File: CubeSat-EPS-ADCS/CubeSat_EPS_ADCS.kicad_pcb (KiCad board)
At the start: 2 copper layers, 92 x 92 mm, 14 parts, among them J1 Conn_01x02_Pin, J2 Conn_01x03_Pin, J3 Conn_01x08_Pin, J4 Conn_01x02_Pin, J5 Screw_Terminal_01x02, J6 Screw_Terminal_01x02, J7 Screw_Terminal_01x02, U1 DRV8833 Module, U2 DRV8833 Module, U4 Buck_LM2596

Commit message: Mostly fine tuning the boards, also added capacitor for battery ADC
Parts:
- added G***: LOGO, Logos:HighVoltage, F.Cu at (142.6, 80.5)
- moved G*** 0.73 mm to (133.0, 138.7)
- moved U4 0.11 mm to (135.1, 61.9)
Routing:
- net GND: track 110.6 -> 131.1 mm
- net VCC_5V: track 14.9 -> 16.2 mm
- net VCC_8.4V_ADCS: track 30.9 -> 31.4 mm
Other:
- board text added: "-Buck LM2596"
- board text added: "-DRV8833"
- board text added: "-Motor 1"
- board text added: "-Motor 2"
- board text added: "-Motor 3"
- board text added: "5V | 1A"
- board text added: "G"
- board text added: "Overvoltage Protection"
- board text added: "S1"
- board text added: "S2"
- board text added: "S3"
- board text added: "S4"
- board text added: "S5"
- board text added: "S6"
- board text added: "VCC"
- board text removed: "M1 M2 M3"
- board text removed: "PWM1"
- board text removed: "PWM2"
- board text removed: "Vm1"
- board text removed: "Vm2"
- board text removed: "Vm3"

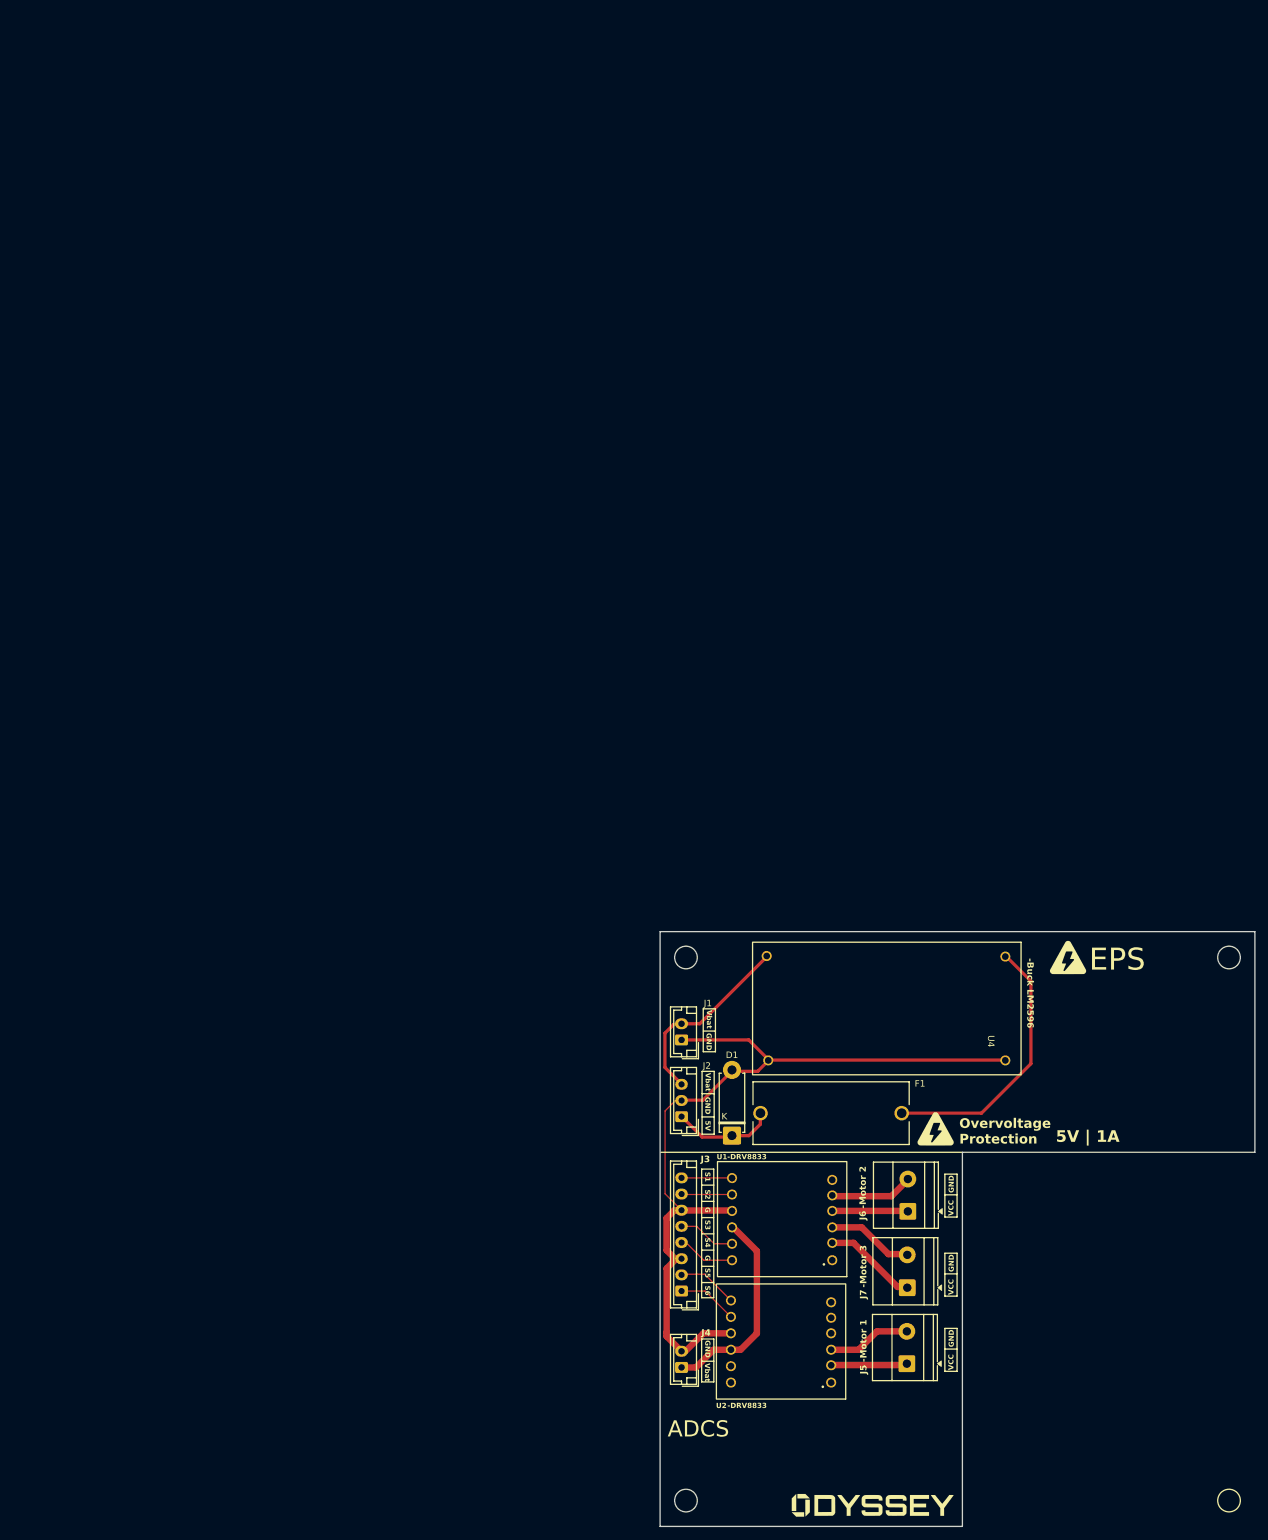
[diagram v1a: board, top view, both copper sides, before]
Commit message: Changing the size of all traces to fit the 1 mm requirement of the draft PCB
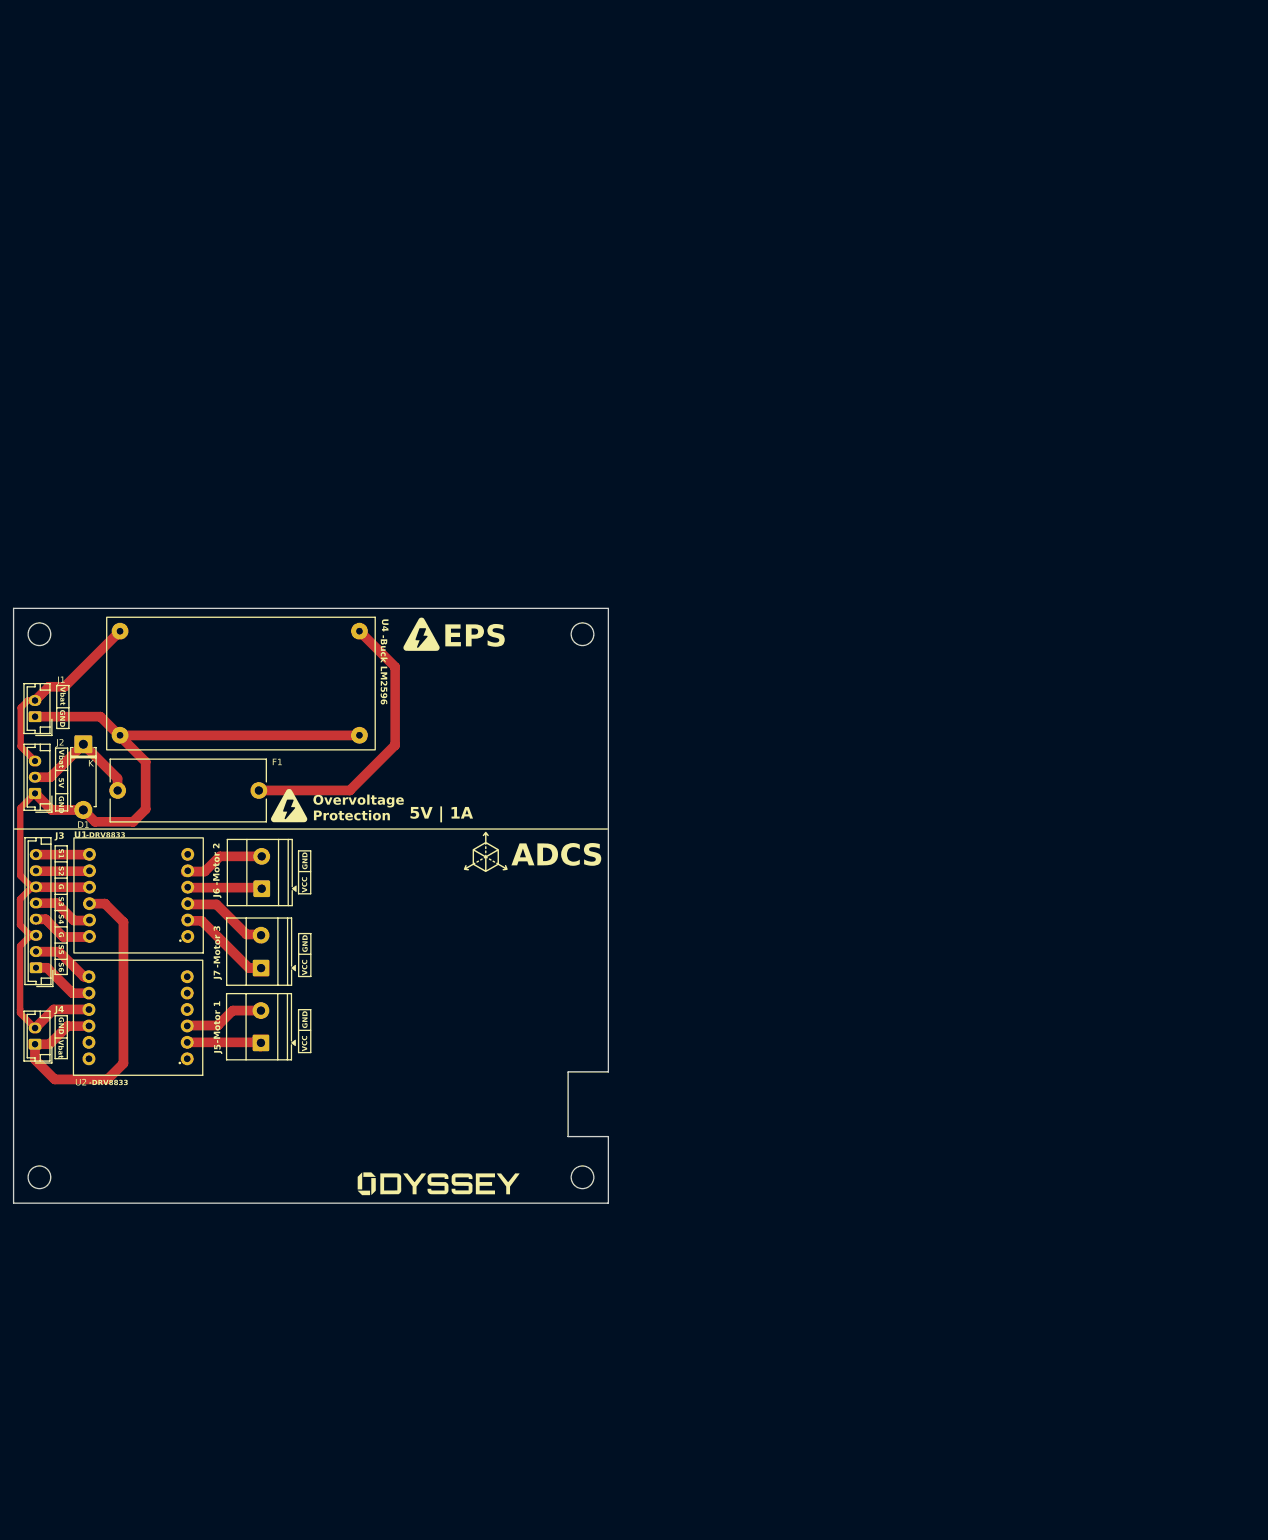
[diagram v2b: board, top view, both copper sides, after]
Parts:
- added G***: LOGO, Logos:Axys, F.Cu at (73.0, 37.7)
- moved D1 117.2 mm to (10.8, 21.0), turned to -90 degrees
- moved U4 111.8 mm to (35.2, 11.6)
- moved G*** 111.8 mm to (42.6, 30.5)
- moved G*** 111.8 mm to (63.1, 4.00)
- moved J1 111.8 mm to (3.32, 16.8)
- moved J2 111.8 mm to (3.32, 28.6)
- moved J4 111.8 mm to (3.32, 67.4)
- moved J6 111.7 mm to (38.4, 43.4)
- moved J3 111.7 mm to (3.47, 55.6)
- moved J5 111.6 mm to (38.3, 67.2)
- moved J7 111.5 mm to (38.3, 55.6)
- moved U1 111.4 mm to (19.3, 44.4)
- moved U2 111.3 mm to (19.3, 63.3)
- moved F1 111.3 mm to (27.0, 28.2)
- moved G*** 83.6 mm to (65.8, 89.0)
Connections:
- J2 pad 1: VCC_5V -> GND
- J2 pad 2: GND -> VCC_5V
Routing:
- net VCC_8.4V_ADCS: track 31.4 -> 56.2 mm
- net GND: track 131.1 -> 147.3 mm
- net VCC_5V: track 16.2 -> 19.0 mm
- net Net-(U4-Vout): track 41.4 -> 44.0 mm
- net VCC_M2: track 12.5 -> 11.3 mm
- net M1_PWM2: track 9.30 -> 9.97 mm
- net M2_PWM2: track 8.94 -> 9.60 mm
- net M2_PWM1: track 8.92 -> 9.58 mm
- net M1_PWM1: track 9.37 -> 9.95 mm
- net VCC_8.4V_EPS: track 29.9 -> 29.4 mm
- net GND_M1: track 12.9 -> 12.4 mm
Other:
- outline, holes or cut-outs redrawn

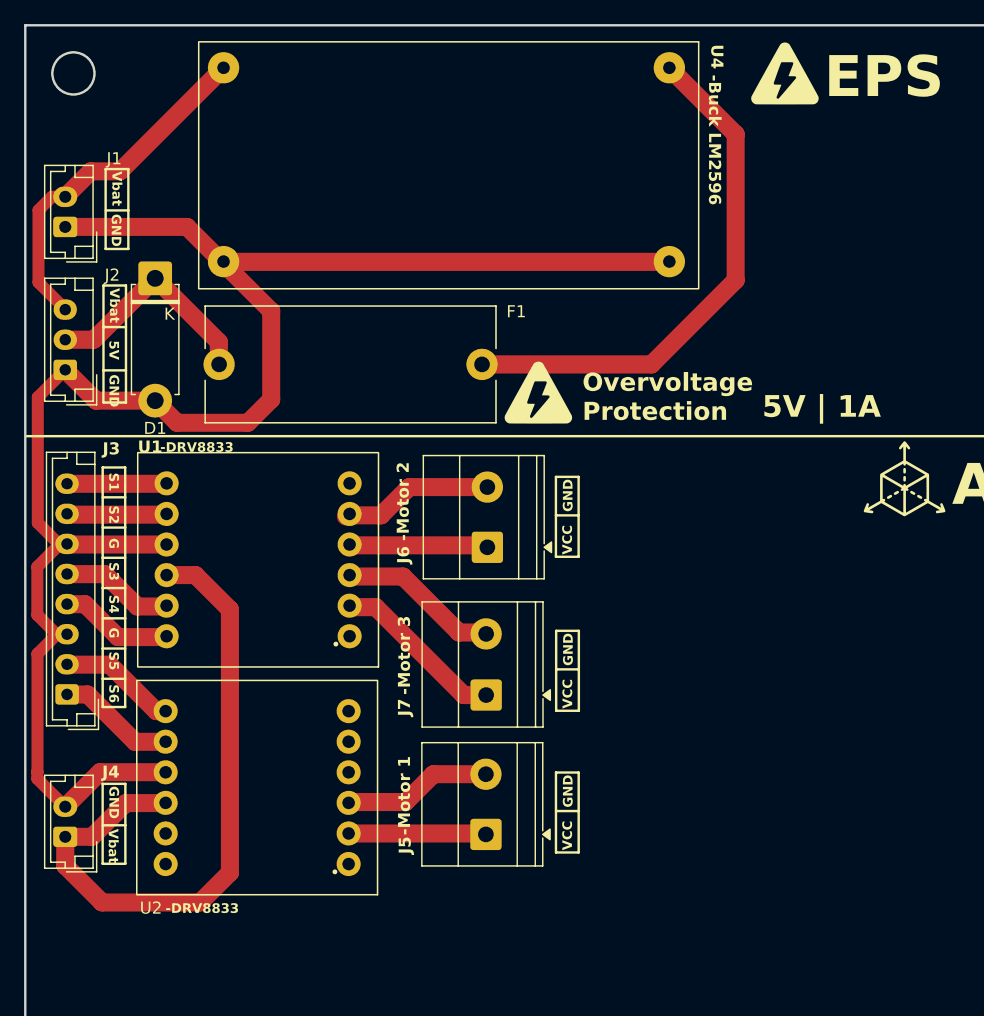
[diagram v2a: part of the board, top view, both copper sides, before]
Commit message: final version of the 3 PCBs, minor size changes for the protoypes
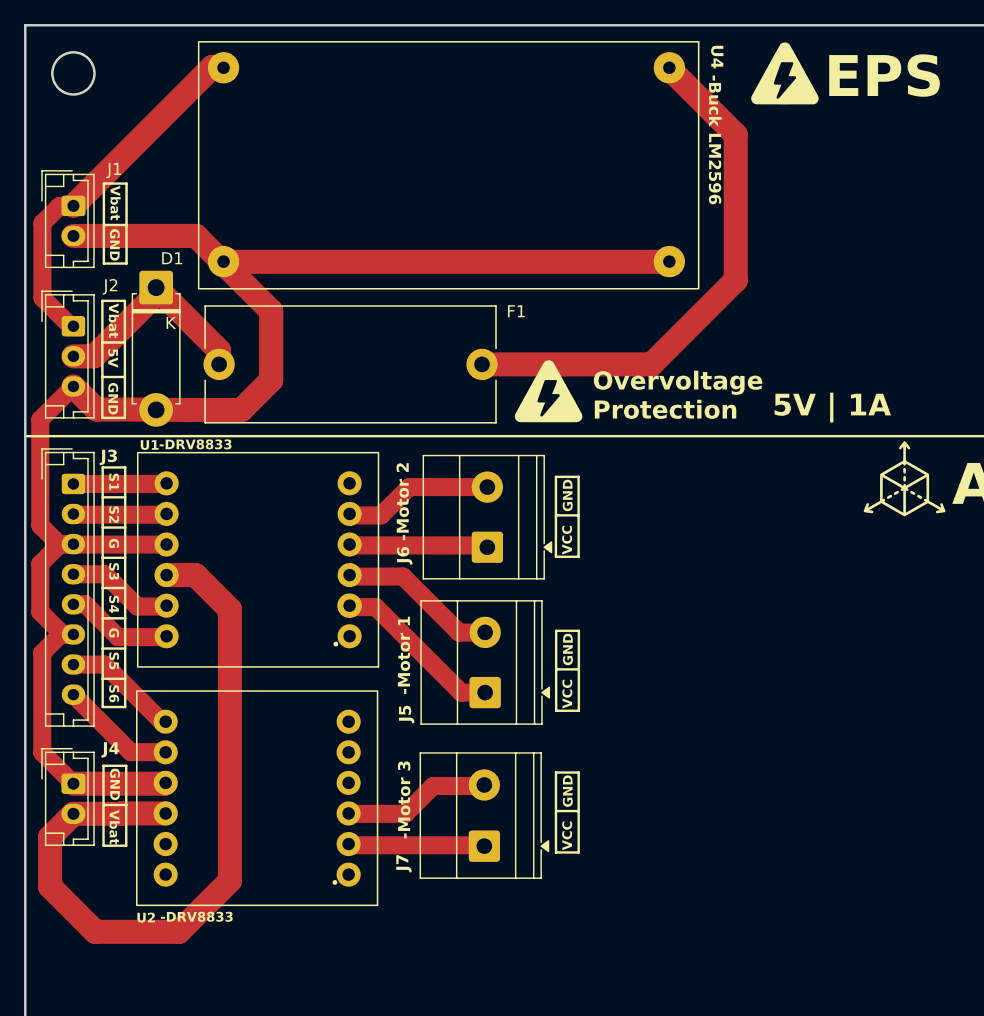
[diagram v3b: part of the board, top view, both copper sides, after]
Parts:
- moved J3 17.5 mm to (4.00, 38.1), turned to -90 degrees
- moved J7 12.6 mm to (38.1, 68.2)
- moved J5 11.8 mm to (38.2, 55.4)
- moved J4 4.46 mm to (4.00, 63.0), turned to -90 degrees
- moved J2 3.68 mm to (4.00, 25.0), turned to -90 degrees
- moved J1 1.88 mm to (4.00, 15.0), turned to -90 degrees
- moved U2 0.88 mm to (19.3, 64.2)
- moved G*** 0.86 mm to (43.5, 30.4)
- moved D1 0.77 mm to (10.9, 21.8)
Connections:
- J1 pad 1: GND -> VCC_8.4V_EPS
- J1 pad 2: VCC_8.4V_EPS -> GND
- J2 pad 1: GND -> VCC_8.4V_EPS
- J2 pad 3: VCC_8.4V_EPS -> GND
- J3 pad 1: M1_PWM2 -> M1_PWM1
- J3 pad 2: M1_PWM1 -> M1_PWM2
- J3 pad 4: M2_PWM2 -> M2_PWM1
- J3 pad 5: M2_PWM1 -> M2_PWM2
- J3 pad 7: M3_PWM2 -> M3_PWM1
- J3 pad 8: M3_PWM1 -> M3_PWM2
- J4 pad 1: VCC_8.4V_ADCS -> GND
- J4 pad 2: GND -> VCC_8.4V_ADCS
- U1 pad 11: M3_PWM2 -> M1_PWM2
- U1 pad 12: M3_PWM1 -> M1_PWM1
- U1 pad 2: VCC_M3 -> VCC_M1
- U1 pad 3: GND_M3 -> GND_M1
- U2 pad 11: M1_PWM2 -> M3_PWM2
- U2 pad 12: M1_PWM1 -> M3_PWM1
- U2 pad 2: VCC_M1 -> VCC_M3
- U2 pad 3: GND_M1 -> GND_M3
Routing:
- net GND: track 147.3 -> 137.7 mm
- net VCC_8.4V_ADCS: track 56.2 -> 61.9 mm
- net VCC_M3: track 14.3 -> 11.3 mm
- net VCC_M1: track 11.8 -> 14.3 mm
- net M1_PWM2: track 9.97 -> 7.79 mm
- net M1_PWM1: track 9.95 -> 7.76 mm
- net M3_PWM1: track 8.44 -> 9.88 mm
- net M3_PWM2: track 8.32 -> 9.65 mm
- net GND_M3: track 13.3 -> 12.3 mm
- net GND_M1: track 12.4 -> 13.3 mm
- net VCC_5V: track 19.0 -> 18.2 mm
- net VCC_8.4V_EPS: track 29.4 -> 30.2 mm
- net M2_PWM1: track 9.58 -> 8.90 mm
- net M2_PWM2: track 9.60 -> 8.92 mm

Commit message: final changes
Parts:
- D1, F1, G*** (x4), J1, J2, J3, J4, J5, J6, J7, U1, U2, U4: moved to B.Cu
- moved J1 84.0 mm to (88.0, 15.0)
- moved J2 84.0 mm to (88.0, 25.0)
- moved J3 84.0 mm to (88.0, 38.1)
- moved J4 84.0 mm to (88.0, 63.0)
- moved D1 70.3 mm to (81.1, 21.8)
- moved G*** 54.1 mm to (19.0, 37.7), turned to 180 degrees
- moved U2 53.5 mm to (72.7, 64.2), turned to 0 degrees
- moved U1 53.3 mm to (72.7, 44.4), turned to 0 degrees
- moved G*** 39.6 mm to (26.2, 89.0), turned to 180 degrees
- moved F1 38.0 mm to (65.0, 28.2), turned to 0 degrees
- moved G*** 34.2 mm to (28.9, 4.00), turned to 180 degrees
- moved U4 21.7 mm to (56.8, 11.6)
- moved J7 15.7 mm to (53.9, 68.2)
- moved J5 15.6 mm to (53.8, 55.4)
- moved J6 15.2 mm to (53.6, 43.4)
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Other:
- outline, holes or cut-outs redrawn

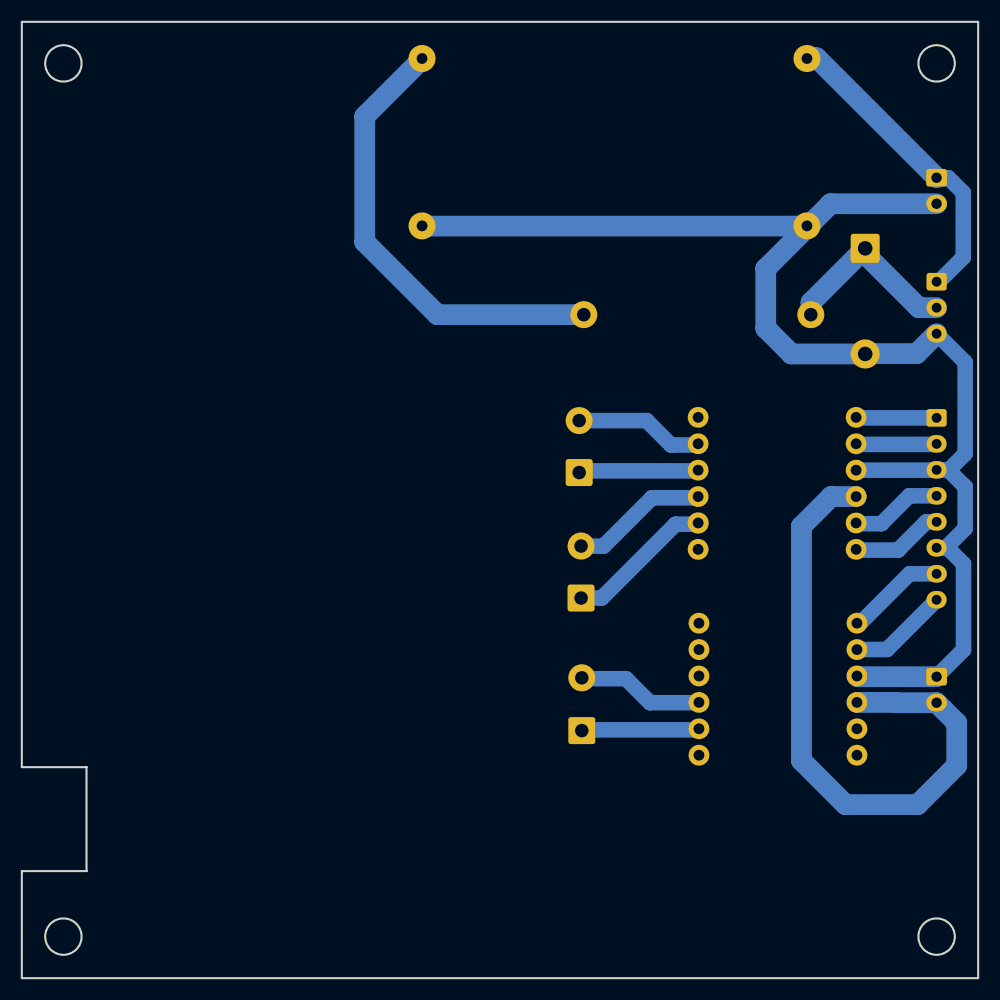
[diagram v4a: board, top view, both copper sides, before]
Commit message: add new drill format
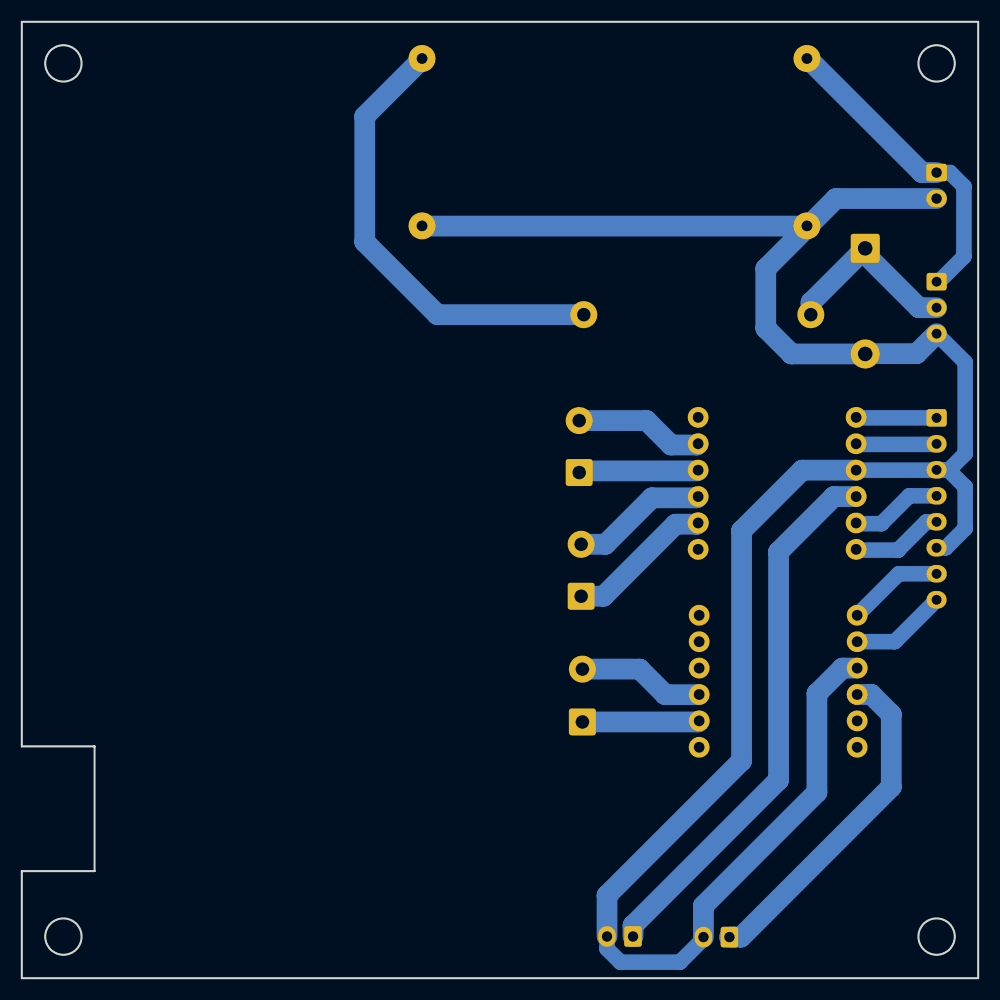
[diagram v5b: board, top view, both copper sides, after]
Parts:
- added J4: Conn_01x02_Pin, Connector_JST:JST_EH_B2B-EH-A_1x02_P2.50mm_Vertical, B.Cu at (68.1, 88.0)
- moved G*** 64.5 mm to (88.4, 72.0), turned to -90 degrees
- moved J5 38.4 mm to (58.8, 88.0), turned to 180 degrees
- moved J8 0.84 mm to (53.9, 67.3)
- moved U2 0.76 mm to (72.8, 63.4)
- moved J1 0.50 mm to (88.0, 14.5)
- moved J6 0.17 mm to (53.8, 55.3)
- renumbered J4 to J5, J5 to J6, J6 to J7, J7 to J8
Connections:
- J5 pad 1: GND -> VCC_8.4V_ADCS
- J5 pad 2: VCC_8.4V_ADCS -> GND
- U2 pad 9: VCC_8.4V_ADCS -> VCC_8.4V_ADCS2
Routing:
- net GND: track 137.7 -> 217.6 mm
- net VCC_8.4V_ADCS2: track 0.00 -> 32.6 mm
- net VCC_8.4V_ADCS: track 61.9 -> 52.5 mm
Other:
- outline, holes or cut-outs redrawn
